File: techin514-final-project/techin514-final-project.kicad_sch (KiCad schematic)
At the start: 6 parts, among them IC1 MPU-6050, U1 MOUDLE-SEEEDUINO-XIAO-ESP32C3, U3 GP2Y0A21YK0F

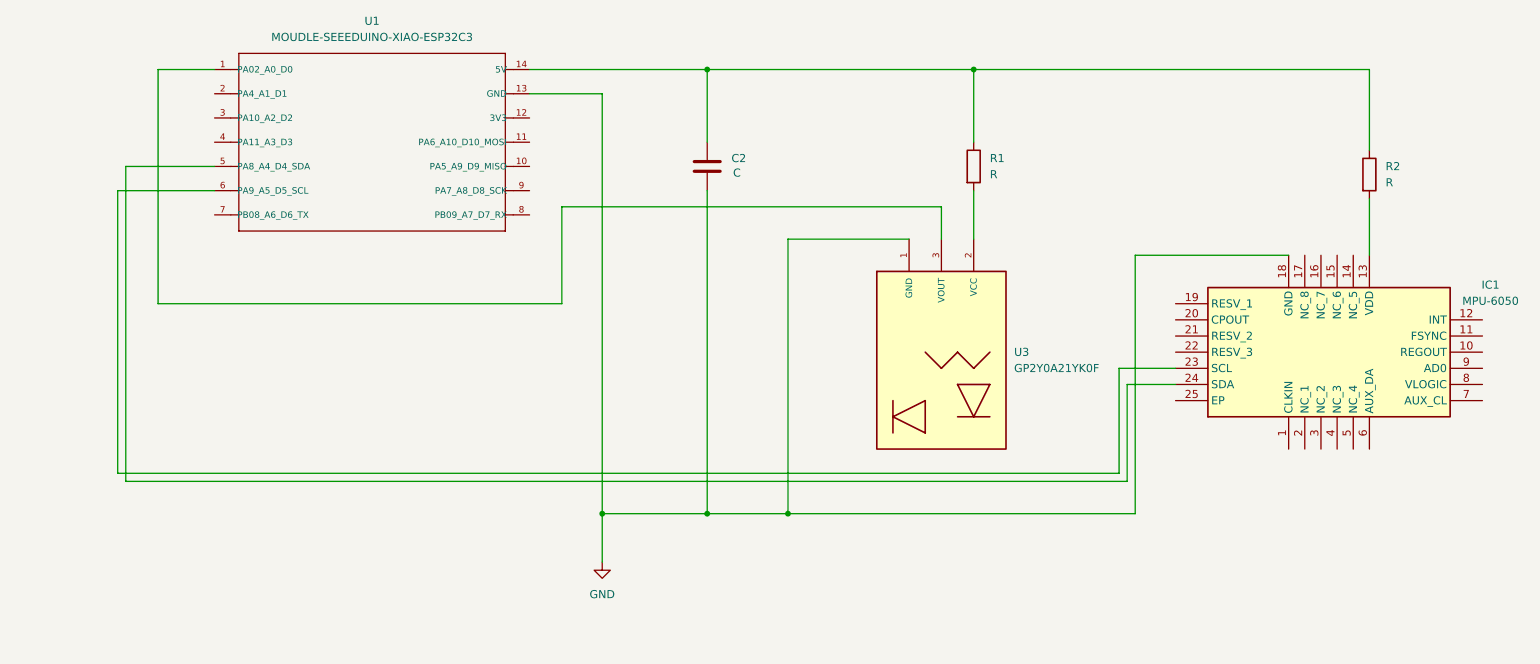
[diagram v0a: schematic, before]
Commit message: Add Battery Datasheet
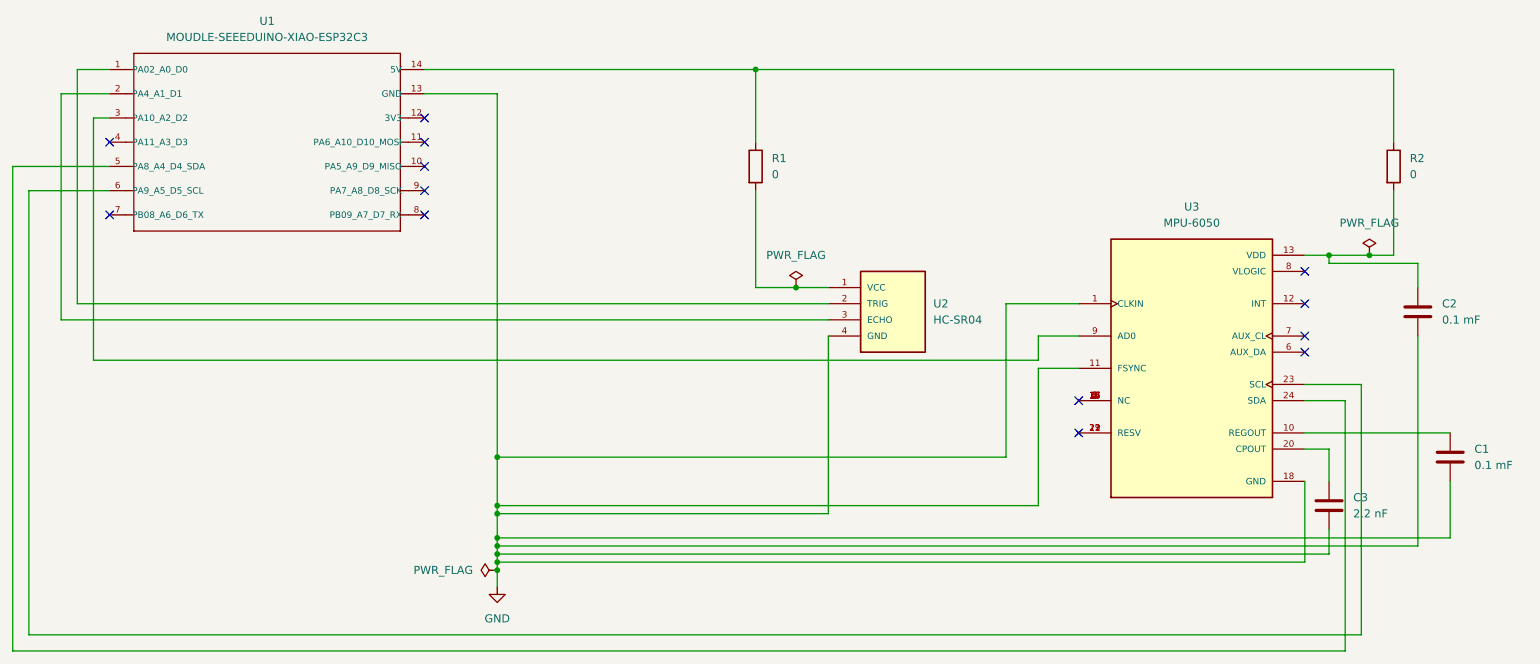
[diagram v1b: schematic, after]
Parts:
- removed IC1: MPU-6050, MPU6050, symbol MPU6050:MPU-6050
- removed U3: GP2Y0A21YK0F, GP2Y0A21YK0F:22-23-2031, symbol GP2Y0A21YK0F:GP2Y0A21YK0F
- added C1: 0.1 mF, Capacitor_SMD:CP_Elec_3x5.3, symbol Device:C
- added C3: 2.2 nF, Capacitor_SMD:CP_Elec_3x5.3, symbol Device:C
- added U2: HC-SR04, 2025_SR04:XCVR_HC-SR04, symbol HC-SR04:HC-SR04
- added U3: MPU-6050, 2025_MPU6050:QFN50P400X400X95-24N, symbol MPU6050:MPU-6050
- C2: value C -> 0.1 mF; footprint (none) -> Capacitor_SMD:CP_Elec_3x5.3
- R1, R2: value R -> 0; footprint (none) -> Resistor_SMD:R_0805_2012Metric_Pad1.20x1.40mm_HandSolder
- U1: footprint MOUDLE14P-SMD-2.54-21X17.8MM -> 2025_XIAO:MOUDLE14P-SMD-2.54-21X17.8MM
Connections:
- net GND: now also C1.2, C3.2, U2.4 (GND), U3.1 (CLKIN), U3.11 (FSYNC), U3.18 (GND)
- net at R2.2: now also C2.1, U3.13 (VDD)
- net at U1.6 (PA9_A5_D5_SCL): now also U3.23 (SCL)
- net at U1.5 (PA8_A4_D4_SDA): now also U3.24 (SDA)
- net at R1.1, R2.1, U1.14 (5V): no longer C2.1
- net at R1.2: now also U2.1 (VCC)
- net at U1.1 (PA02_A0_D0): now also U2.2 (TRIG)
- net at U1.2 (PA4_A1_D1): now also U2.3 (ECHO)
- net at U1.3 (PA10_A2_D2): now also U3.9 (AD0)
- new net: C1.1, U3.10 (REGOUT)
- new net: U3.14 (NC), U3.15 (NC), U3.16 (NC), U3.17 (NC), U3.2 (NC), U3.3 (NC), U3.4 (NC), U3.5 (NC)
- new net: U3.19 (RESV), U3.21 (RESV), U3.22 (RESV)
- new net: C3.1, U3.20 (CPOUT)
- no-connect marks 0 -> 13
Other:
- title: (none) -> TECHIN514 Final Project Sensor Circuit
- moved on the sheet: R1, R2, U1

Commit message: Add sensor code
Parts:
- removed C1, C2: 0.1 mF, Capacitor_SMD:CP_Elec_3x5.3, symbol Device:C
- removed C3: 2.2 nF, Capacitor_SMD:CP_Elec_3x5.3, symbol Device:C
- removed U2: HC-SR04, 2025_SR04:XCVR_HC-SR04, symbol HC-SR04:HC-SR04
- removed U3: MPU-6050, 2025_MPU6050:QFN50P400X400X95-24N, symbol MPU6050:MPU-6050
- added BT1: Battery_Cell, Connector_JST:JST_PH_B2B-PH-K_1x02_P2.00mm_Vertical, symbol Device:Battery_Cell
- added D1, D2: LED, LED_THT:LED_D5.0mm, symbol Device:LED
- added J1: Conn_01x02_Pin, Connector_JST:JST_PH_B2B-PH-K_1x02_P2.00mm_Vertical, symbol Connector:Conn_01x02_Pin
- added M1: Stepper_Motor_bipolar, 2025_X27_168:x27_stepper_two_holes, symbol Motor:Stepper_Motor_bipolar
- added SW1: SW_SPDT, Connector_JST:JST_EH_B3B-EH-A_1x03_P2.50mm_Vertical, symbol Switch:SW_SPDT
- R1, R2: value 0 -> R; footprint Resistor_SMD:R_0805_2012Metric_Pad1.20x1.40mm_HandSolder -> Resistor_THT:R_Axial_DIN0207_L6.3mm_D2.5mm_P15.24mm_Horizontal
- U1: footprint 2025_XIAO:MOUDLE14P-SMD-2.54-21X17.8MM -> 2025_XIAO:XIAO_ESP32_SENSE
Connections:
- net GND: now also BT1.2 (-), D1.1 (K), D2.1 (K), J1.2 (Pin_2)
- net at R1.2: now also D1.2 (A)
- net at U1.1 (PA02_A0_D0): now also M1.1
- net at U1.2 (PA4_A1_D1): now also M1.2 (-)
- net at R2.2: now also D2.2 (A)
- net at U1.5 (PA8_A4_D4_SDA): now also R2.1
- net at U1.3 (PA10_A2_D2): now also M1.3
- net at U1.12 (3V3): now also R1.1, J1.1 (Pin_1), SW1.3 (C)
- net at U1.4 (PA11_A3_D3): now also M1.4
- new net: BT1.1 (+), SW1.2 (B)
- now unconnected: U1.14 (5V)
- no-connect marks 13 -> 8
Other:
- moved on the sheet: U1
